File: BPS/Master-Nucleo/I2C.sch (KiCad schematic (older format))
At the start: 5 parts, among them J14 Conn_01x03, U8 M24128

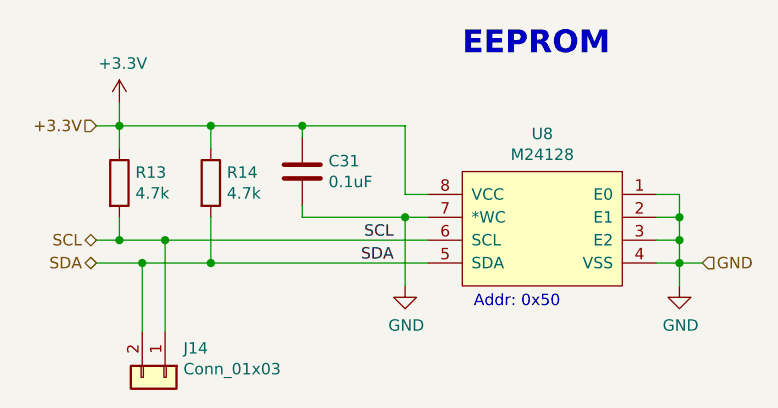
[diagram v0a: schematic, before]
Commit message: Adds Nucleo version of master board.
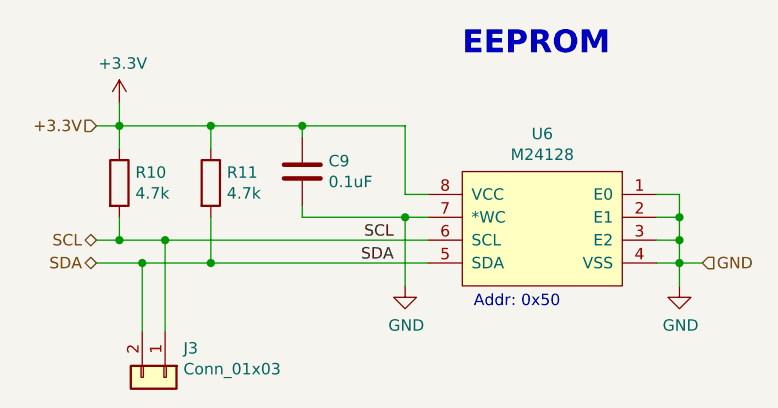
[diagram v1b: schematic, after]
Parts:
- renumbered C31 to C9, J14 to J3, R13 to R10, R14 to R11, U8 to U6
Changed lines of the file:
@@
 EESchema Schematic File Version 4
-LIBS:BPSMaster-cache
 EELAYER 29 0
 EELAYER END
@@
 GND
 $Comp
-L utsvt-bps:M24128 U8
+L utsvt-bps:M24128 U6
 U 1 1 5C3511BE
 P 4250 2800
-F 0 "U8" H 4250 2965 50  0000 C CNN
+F 0 "U6" H 4250 2965 50  0000 C CNN
 F 1 "M24128" H 4250 2874 50  0000 C CNN
 F 2 "UTSVT_BPS:M24128-BRMN6P" H 4250 2800 50  0001 C CNN
@@
 +3.3V
 $Comp
-L Device:C C31
+L Device:C C9
 U 1 1 5C35143C
 P 3200 2800
-F 0 "C31" H 3315 2846 50  0000 L CNN
+F 0 "C9" H 3315 2846 50  0000 L CNN
 F 1 "0.1uF" H 3315 2755 50  0000 L CNN
 F 2 "Capacitor_SMD:C_0805_2012Metric" H 3238 2650 50  0001 C CNN
@@
 $EndComp
 $Comp
-L power:GND #PWR060
+L power:GND #PWR0122
 U 1 1 5C3514DC
 P 4850 3300
-F 0 "#PWR060" H 4850 3050 50  0001 C CNN
+F 0 "#PWR0122" H 4850 3050 50  0001 C CNN
 F 1 "GND" H 4855 3127 50  0000 C CNN
 F 2 "" H 4850 3300 50  0001 C CNN
@@
 	4850 3200 4950 3200
 $Comp
-L power:GND #PWR059
+L power:GND #PWR0123
 U 1 1 5C3516F5
 P 3650 3300
-F 0 "#PWR059" H 3650 3050 50  0001 C CNN
+F 0 "#PWR0123" H 3650 3050 50  0001 C CNN
 F 1 "GND" H 3655 3127 50  0000 C CNN
 F 2 "" H 3650 3300 50  0001 C CNN
@@
 	3650 3000 3750 3000
 $Comp
-L Device:R R14
+L Device:R R11
 U 1 1 5C351986
 P 2800 2850
-F 0 "R14" H 2870 2896 50  0000 L CNN
+F 0 "R11" H 2870 2896 50  0000 L CNN
 F 1 "4.7k" H 2870 2805 50  0000 L CNN
 F 2 "Resistor_SMD:R_0805_2012Metric" V 2730 2850 50  0001 C CNN
@@
 $EndComp
 $Comp
-L Device:R R13
+L Device:R R10
 U 1 1 5C3519B6
 P 2400 2850
-F 0 "R13" H 2470 2896 50  0000 L CNN
+F 0 "R10" H 2470 2896 50  0000 L CNN
 F 1 "4.7k" H 2470 2805 50  0000 L CNN
 F 2 "Resistor_SMD:R_0805_2012Metric" V 2330 2850 50  0001 C CNN
@@
 $EndComp
 $Comp
-L power:+3.3V #PWR055
+L power:+3.3V #PWR0124
 U 1 1 5C351A76
 P 2400 2500
-F 0 "#PWR055" H 2400 2350 50  0001 C CNN
+F 0 "#PWR0124" H 2400 2350 50  0001 C CNN
 F 1 "+3.3V" H 2415 2673 50  0000 C CNN
 F 2 "" H 2400 2500 50  0001 C CNN
@@
 	4850 3100 4850 3000
 $Comp
-L Connector_Generic:Conn_01x02 J14
+L Connector_Generic:Conn_01x02 J3
 U 1 1 5C646686
 P 2600 3700
-F 0 "J14" V 2473 3780 50  0000 L CNN
+F 0 "J3" V 2473 3780 50  0000 L CNN
 F 1 "Conn_01x03" V 2564 3780 50  0000 L CNN
 F 2 "Connector_PinHeader_2.54mm:PinHeader_1x02_P2.54mm_Vertical" H 2600 3700 50  0001 C CNN
